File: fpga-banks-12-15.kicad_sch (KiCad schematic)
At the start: 1 part, among them U15 XC7K160T-FFG676

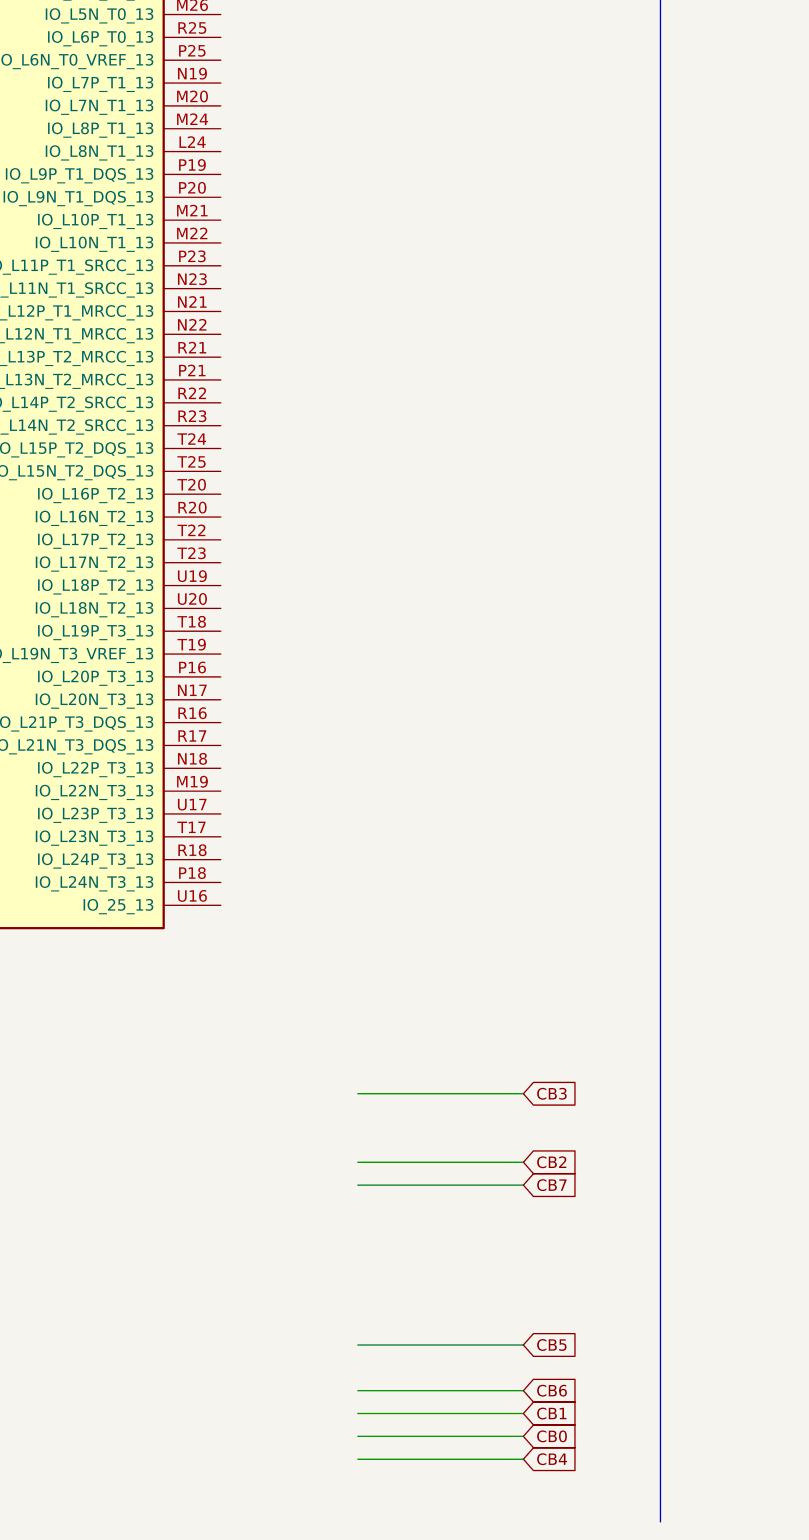
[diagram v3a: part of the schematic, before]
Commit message: Finish assigment and routing of ECC die
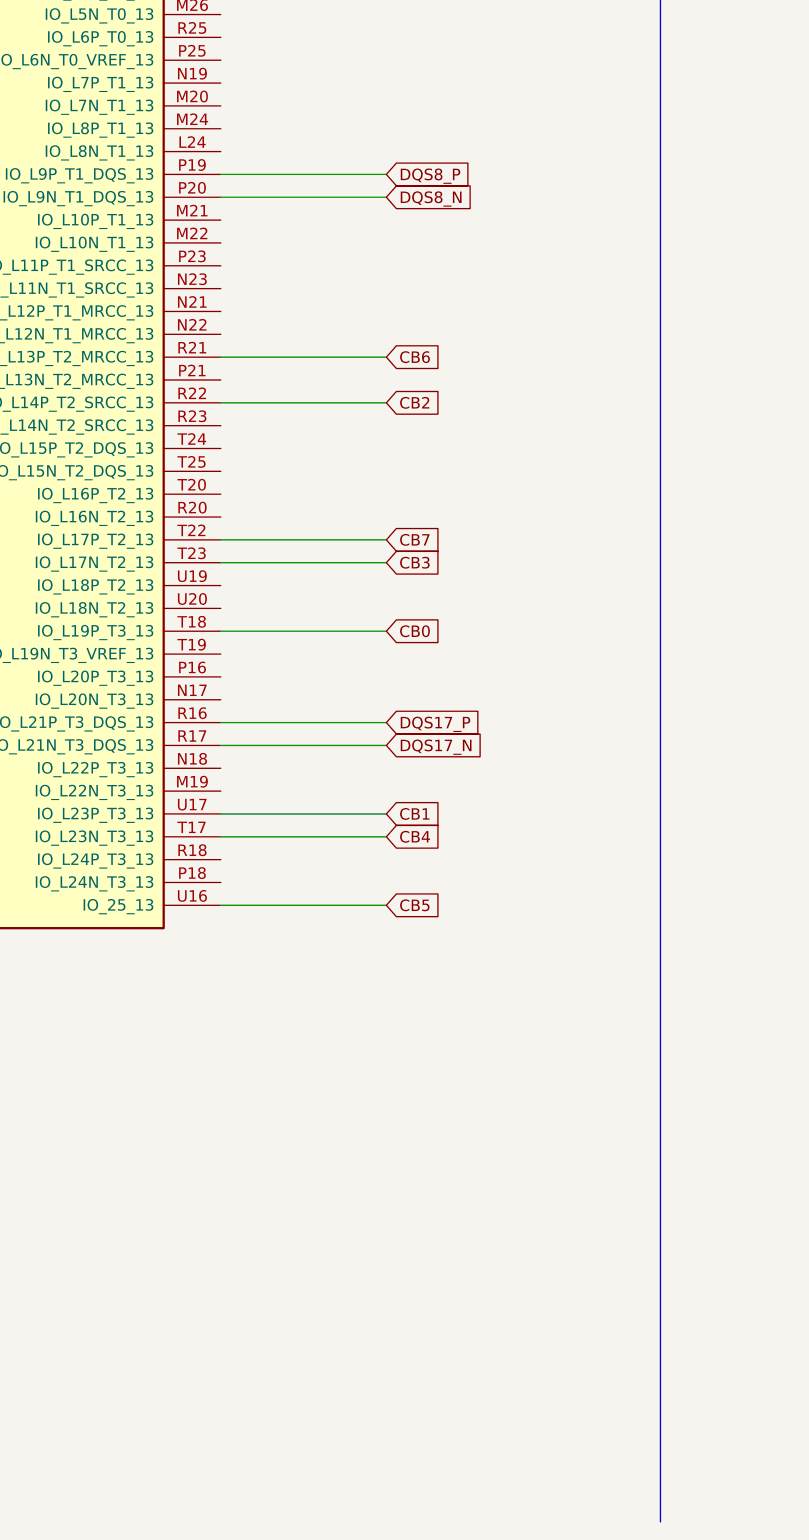
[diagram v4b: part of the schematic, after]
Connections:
- net CB0: now also U15.T18 (IO_L19P_T3_13)
- net CB1: now also U15.U17 (IO_L23P_T3_13)
- net CB2: now also U15.R22 (IO_L14P_T2_SRCC_13)
- net CB3: now also U15.T23 (IO_L17N_T2_13)
- net CB4: now also U15.T17 (IO_L23N_T3_13)
- net CB5: now also U15.U16 (IO_25_13)
- net CB6: now also U15.R21 (IO_L13P_T2_MRCC_13)
- net CB7: now also U15.T22 (IO_L17P_T2_13)
- net DQS8_P: now reaches U15.P19 (IO_L9P_T1_DQS_13)
- net DQS8_N: now reaches U15.P20 (IO_L9N_T1_DQS_13)
- net DQS17_P: now reaches U15.R16 (IO_L21P_T3_DQS_13)
- net DQS17_N: now reaches U15.R17 (IO_L21N_T3_DQS_13)
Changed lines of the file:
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@@
     (stroke (width 0) (type default) (color 0 0 0 0))
   )
-  (wire (pts (xy 176.53 278.13) (xy 194.945 278.13))
+  (wire (pts (xy 161.29 208.915) (xy 179.705 208.915))
     (stroke (width 0) (type default) (color 0 0 0 0))
   )
@@
     (stroke (width 0) (type default) (color 0 0 0 0))
   )
-  (wire (pts (xy 176.53 270.51) (xy 194.945 270.51))
+  (wire (pts (xy 161.29 155.575) (xy 179.705 155.575))
+    (stroke (width 0) (type default) (color 0 0 0 0))
+  )
+  (wire (pts (xy 161.29 135.255) (xy 179.705 135.255))
     (stroke (width 0) (type default) (color 0 0 0 0))
   )
@@
     (stroke (width 0) (type default) (color 0 0 0 0))
   )
+  (wire (pts (xy 161.29 198.755) (xy 179.705 198.755))
+    (stroke (width 0) (type default) (color 0 0 0 0))
+  )
   (wire (pts (xy 82.55 66.04) (xy 85.09 66.04))
     (stroke (width 0) (type default) (color 0 0 0 0))
@@
     (stroke (width 0) (type default) (color 0 0 0 0))
   )
-  (wire (pts (xy 176.53 275.59) (xy 194.945 275.59))
+  (wire (pts (xy 161.29 186.055) (xy 179.705 186.055))
     (stroke (width 0) (type default) (color 0 0 0 0))
   )
@@
     (stroke (width 0) (type default) (color 0 0 0 0))
   )
-  (wire (pts (xy 176.53 265.43) (xy 194.945 265.43))
+  (wire (pts (xy 161.29 216.535) (xy 179.705 216.535))
     (stroke (width 0) (type default) (color 0 0 0 0))
   )
@@
     (stroke (width 0) (type default) (color 0 0 0 0))
   )
+  (wire (pts (xy 161.29 137.795) (xy 179.705 137.795))
+    (stroke (width 0) (type default) (color 0 0 0 0))
+  )
   (wire (pts (xy 348.615 60.96) (xy 348.615 66.675))
     (stroke (width 0) (type default) (color 0 0 0 0))
@@
     (stroke (width 0) (type default) (color 0 0 0 0))
   )
-  (wire (pts (xy 176.53 247.65) (xy 194.945 247.65))
+  (wire (pts (xy 161.29 175.895) (xy 179.705 175.895))
     (stroke (width 0) (type default) (color 0 0 0 0))
   )
@@
     (stroke (width 0) (type default) (color 0 0 0 0))
   )
-  (wire (pts (xy 176.53 237.49) (xy 194.945 237.49))
+  (wire (pts (xy 161.29 178.435) (xy 179.705 178.435))
     (stroke (width 0) (type default) (color 0 0 0 0))
   )
@@
     (stroke (width 0) (type default) (color 0 0 0 0))
   )
+  (wire (pts (xy 161.29 196.215) (xy 179.705 196.215))
+    (stroke (width 0) (type default) (color 0 0 0 0))
+  )
   (wire (pts (xy 154.94 60.96) (xy 154.94 66.04))
     (stroke (width 0) (type default) (color 0 0 0 0))
@@
     (stroke (width 0) (type default) (color 0 0 0 0))
   )
-  (wire (pts (xy 176.53 245.11) (xy 194.945 245.11))
+  (wire (pts (xy 161.29 160.655) (xy 179.705 160.655))
     (stroke (width 0) (type default) (color 0 0 0 0))
   )
@@
     (stroke (width 0) (type default) (color 0 0 0 0))
   )
-  (wire (pts (xy 176.53 273.05) (xy 194.945 273.05))
+  (wire (pts (xy 161.29 206.375) (xy 179.705 206.375))
     (stroke (width 0) (type default) (color 0 0 0 0))
   )
@@
     )
   )
-  (global_label "CB6" (shape input) (at 194.945 270.51 0) (fields_autoplaced)
+  (global_label "CB6" (shape input) (at 179.705 155.575 0) (fields_autoplaced)
     (effects (font (size 1.27 1.27)) (justify left))
-    (property "Intersheet References" "${INTERSHEET_REFS}" (id 0) (at -177.165 76.835 0)
+    (property "Intersheet References" "${INTERSHEET_REFS}" (id 0) (at -192.405 -38.1 0)
       (effects (font (size 1.27 1.27)) hide)
     )
@@
     )
   )
-  (global_label "CB5" (shape input) (at 194.945 265.43 0) (fields_autoplaced)
+  (global_label "CB5" (shape input) (at 179.705 216.535 0) (fields_autoplaced)
     (effects (font (size 1.27 1.27)) (justify left))
-    (property "Intersheet References" "${INTERSHEET_REFS}" (id 0) (at -177.165 76.835 0)
+    (property "Intersheet References" "${INTERSHEET_REFS}" (id 0) (at -192.405 27.94 0)
       (effects (font (size 1.27 1.27)) hide)
     )
@@
     )
   )
-  (global_label "CB0" (shape input) (at 194.945 275.59 0) (fields_autoplaced)
+  (global_label "CB0" (shape input) (at 179.705 186.055 0) (fields_autoplaced)
     (effects (font (size 1.27 1.27)) (justify left))
-    (property "Intersheet References" "${INTERSHEET_REFS}" (id 0) (at -177.165 76.835 0)
+    (property "Intersheet References" "${INTERSHEET_REFS}" (id 0) (at -192.405 -12.7 0)
       (effects (font (size 1.27 1.27)) hide)
     )
@@
     )
   )
-  (global_label "CB7" (shape input) (at 194.945 247.65 0) (fields_autoplaced)
+  (global_label "CB7" (shape input) (at 179.705 175.895 0) (fields_autoplaced)
     (effects (font (size 1.27 1.27)) (justify left))
-    (property "Intersheet References" "${INTERSHEET_REFS}" (id 0) (at -177.165 76.835 0)
+    (property "Intersheet References" "${INTERSHEET_REFS}" (id 0) (at -192.405 5.08 0)
       (effects (font (size 1.27 1.27)) hide)
     )
@@
     (property "Intersheet References" "${INTERSHEET_REFS}" (id 0) (at 0 0 0)
       (effects (font (size 1.27 1.27)) hide)
+    )
+  )
+  (global_label "DQS17_N" (shape input) (at 179.705 198.755 0) (fields_autoplaced)
+    (effects (font (size 1.27 1.27)) (justify left))
+    (property "Intersheet References" "${INTERSHEET_REFS}" (id 0) (at 190.5563 198.6756 0)
+      (effects (font (size 1.27 1.27)) (justify left) hide)
     )
   )
@@
     )
   )
+  (global_label "DQS8_N" (shape input) (at 179.705 137.795 0) (fields_autoplaced)
+    (effects (font (size 1.27 1.27)) (justify left))
+    (property "Intersheet References" "${INTERSHEET_REFS}" (id 0) (at 189.3468 137.7156 0)
+      (effects (font (size 1.27 1.27)) (justify left) hide)
+    )
+  )
   (global_label "HR_DQ7" (shape input) (at 59.69 173.355 180) (fields_autoplaced)
     (effects (font (size 1.27 1.27)) (justify right))
@@
     )
   )
-  (global_label "CB4" (shape input) (at 194.945 278.13 0) (fields_autoplaced)
+  (global_label "CB4" (shape input) (at 179.705 208.915 0) (fields_autoplaced)
     (effects (font (size 1.27 1.27)) (justify left))
-    (property "Intersheet References" "${INTERSHEET_REFS}" (id 0) (at -177.165 76.835 0)
-      (effects (font (size 1.27 1.27)) hide)
-    )
-  )
-  (global_label "CB2" (shape input) (at 194.945 245.11 0) (fields_autoplaced)
+    (property "Intersheet References" "${INTERSHEET_REFS}" (id 0) (at -192.405 7.62 0)
+      (effects (font (size 1.27 1.27)) hide)
+    )
+  )
+  (global_label "CB2" (shape input) (at 179.705 160.655 0) (fields_autoplaced)
     (effects (font (size 1.27 1.27)) (justify left))
-    (property "Intersheet References" "${INTERSHEET_REFS}" (id 0) (at -177.165 76.835 0)
+    (property "Intersheet References" "${INTERSHEET_REFS}" (id 0) (at -192.405 -7.62 0)
       (effects (font (size 1.27 1.27)) hide)
     )
@@
     )
   )
+  (global_label "DQS17_P" (shape input) (at 179.705 196.215 0) (fields_autoplaced)
+    (effects (font (size 1.27 1.27)) (justify left))
+    (property "Intersheet References" "${INTERSHEET_REFS}" (id 0) (at 190.4959 196.1356 0)
+      (effects (font (size 1.27 1.27)) (justify left) hide)
+    )
+  )
   (global_label "USR_LED2" (shape input) (at 253.365 130.81 180) (fields_autoplaced)
     (effects (font (size 1.27 1.27)) (justify right))
@@
     )
   )
-  (global_label "CB1" (shape input) (at 194.945 273.05 0) (fields_autoplaced)
+  (global_label "CB1" (shape input) (at 179.705 206.375 0) (fields_autoplaced)
     (effects (font (size 1.27 1.27)) (justify left))
-    (property "Intersheet References" "${INTERSHEET_REFS}" (id 0) (at -177.165 76.835 0)
+    (property "Intersheet References" "${INTERSHEET_REFS}" (id 0) (at -192.405 10.16 0)
       (effects (font (size 1.27 1.27)) hide)
     )
@@
     )
   )
-  (global_label "CB3" (shape input) (at 194.945 237.49 0) (fields_autoplaced)
+  (global_label "CB3" (shape input) (at 179.705 178.435 0) (fields_autoplaced)
     (effects (font (size 1.27 1.27)) (justify left))
-    (property "Intersheet References" "${INTERSHEET_REFS}" (id 0) (at -177.165 76.835 0)
+    (property "Intersheet References" "${INTERSHEET_REFS}" (id 0) (at -192.405 17.78 0)
       (effects (font (size 1.27 1.27)) hide)
     )
@@
     )
   )
+  (global_label "DQS8_P" (shape input) (at 179.705 135.255 0) (fields_autoplaced)
+    (effects (font (size 1.27 1.27)) (justify left))
+    (property "Intersheet References" "${INTERSHEET_REFS}" (id 0) (at 189.2863 135.1756 0)
+      (effects (font (size 1.27 1.27)) (justify left) hide)
+    )
+  )

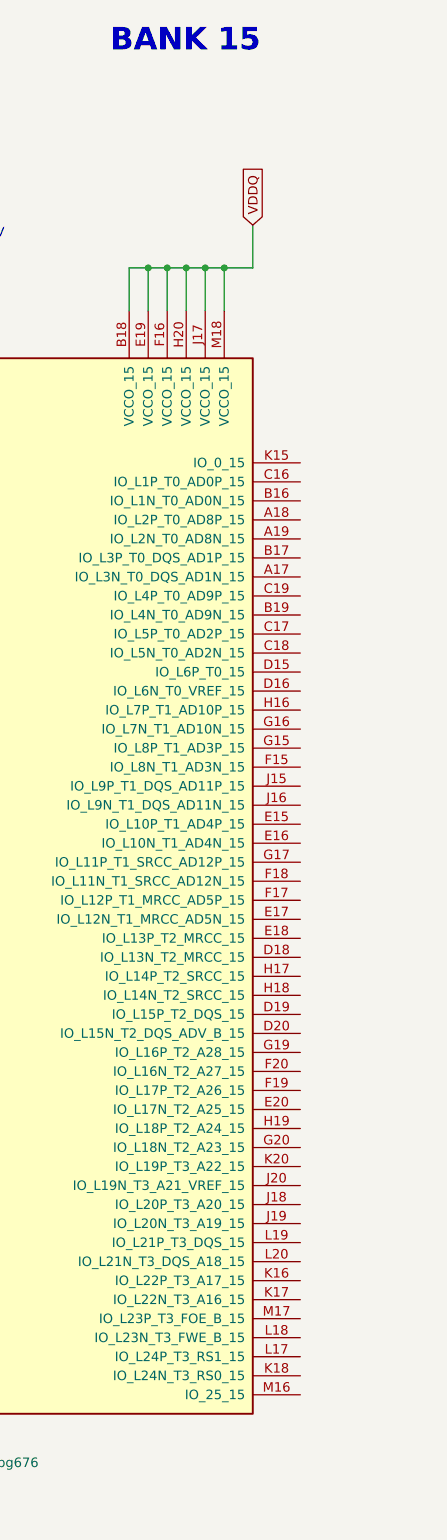
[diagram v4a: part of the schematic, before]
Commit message: Implement LED and PB mechanical concept. Assign bank 15 to FMC, remove buttons and add new ones
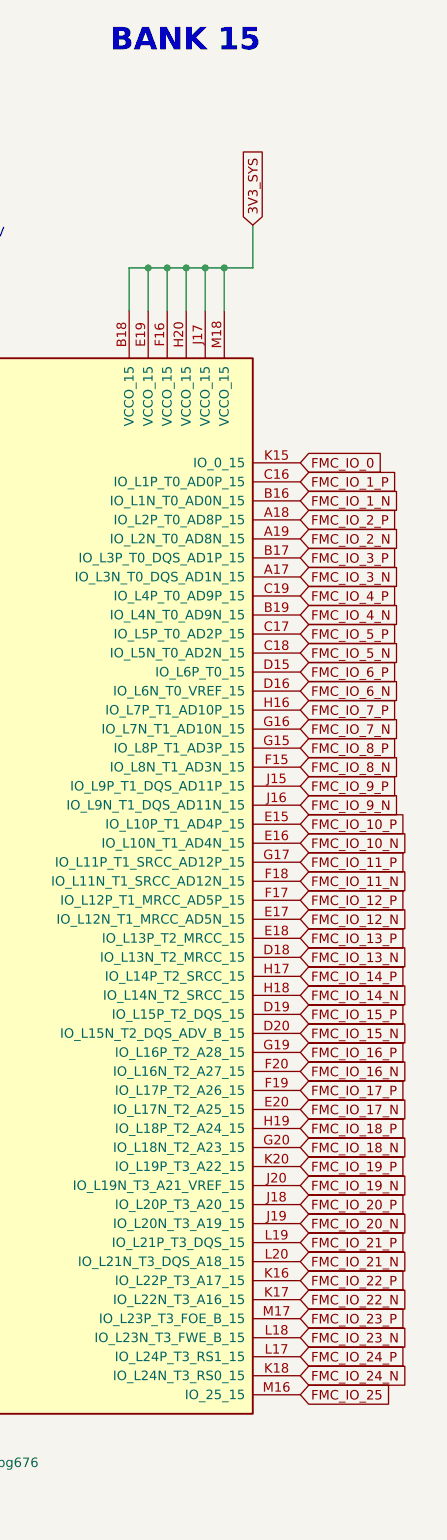
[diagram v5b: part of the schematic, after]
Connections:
- net 3V3_SYS: now also U15.B18 (VCCO_15), U15.E19 (VCCO_15), U15.F16 (VCCO_15), U15.H20 (VCCO_15), U15.J17 (VCCO_15), U15.M18 (VCCO_15)
- net VDDQ: no longer U15.B18 (VCCO_15), U15.E19 (VCCO_15), U15.F16 (VCCO_15), U15.H20 (VCCO_15), U15.J17 (VCCO_15), U15.M18 (VCCO_15)
- net FMC_IO_3_N: now reaches U15.A17 (IO_L3N_T0_DQS_AD1N_15)
- net FMC_IO_2_P: now reaches U15.A18 (IO_L2P_T0_AD8P_15)
- net FMC_IO_2_N: now reaches U15.A19 (IO_L2N_T0_AD8N_15)
- net FMC_IO_1_N: now reaches U15.B16 (IO_L1N_T0_AD0N_15)
- net FMC_IO_3_P: now reaches U15.B17 (IO_L3P_T0_DQS_AD1P_15)
- net FMC_IO_4_N: now reaches U15.B19 (IO_L4N_T0_AD9N_15)
- net FMC_IO_1_P: now reaches U15.C16 (IO_L1P_T0_AD0P_15)
- net FMC_IO_5_P: now reaches U15.C17 (IO_L5P_T0_AD2P_15)
- net FMC_IO_5_N: now reaches U15.C18 (IO_L5N_T0_AD2N_15)
- net FMC_IO_4_P: now reaches U15.C19 (IO_L4P_T0_AD9P_15)
- net FMC_IO_6_P: now reaches U15.D15 (IO_L6P_T0_15)
- net FMC_IO_6_N: now reaches U15.D16 (IO_L6N_T0_VREF_15)
- net FMC_IO_13_N: now reaches U15.D18 (IO_L13N_T2_MRCC_15)
- net FMC_IO_15_P: now reaches U15.D19 (IO_L15P_T2_DQS_15)
- net FMC_IO_15_N: now reaches U15.D20 (IO_L15N_T2_DQS_ADV_B_15)
- net FMC_IO_10_P: now reaches U15.E15 (IO_L10P_T1_AD4P_15)
- net FMC_IO_10_N: now reaches U15.E16 (IO_L10N_T1_AD4N_15)
- net FMC_IO_12_N: now reaches U15.E17 (IO_L12N_T1_MRCC_AD5N_15)
- net FMC_IO_13_P: now reaches U15.E18 (IO_L13P_T2_MRCC_15)
- net FMC_IO_17_N: now reaches U15.E20 (IO_L17N_T2_A25_15)
- net FMC_IO_8_N: now reaches U15.F15 (IO_L8N_T1_AD3N_15)
- net FMC_IO_12_P: now reaches U15.F17 (IO_L12P_T1_MRCC_AD5P_15)
- net FMC_IO_11_N: now reaches U15.F18 (IO_L11N_T1_SRCC_AD12N_15)
- net FMC_IO_17_P: now reaches U15.F19 (IO_L17P_T2_A26_15)
- net FMC_IO_16_N: now reaches U15.F20 (IO_L16N_T2_A27_15)
- net FMC_IO_8_P: now reaches U15.G15 (IO_L8P_T1_AD3P_15)
- net FMC_IO_7_N: now reaches U15.G16 (IO_L7N_T1_AD10N_15)
- net FMC_IO_11_P: now reaches U15.G17 (IO_L11P_T1_SRCC_AD12P_15)
- net FMC_IO_16_P: now reaches U15.G19 (IO_L16P_T2_A28_15)
- net FMC_IO_18_N: now reaches U15.G20 (IO_L18N_T2_A23_15)
- net FMC_IO_7_P: now reaches U15.H16 (IO_L7P_T1_AD10P_15)
- net FMC_IO_14_P: now reaches U15.H17 (IO_L14P_T2_SRCC_15)
- net FMC_IO_14_N: now reaches U15.H18 (IO_L14N_T2_SRCC_15)
- net FMC_IO_18_P: now reaches U15.H19 (IO_L18P_T2_A24_15)
- net FMC_IO_9_P: now reaches U15.J15 (IO_L9P_T1_DQS_AD11P_15)
- net FMC_IO_9_N: now reaches U15.J16 (IO_L9N_T1_DQS_AD11N_15)
- net FMC_IO_20_P: now reaches U15.J18 (IO_L20P_T3_A20_15)
- net FMC_IO_20_N: now reaches U15.J19 (IO_L20N_T3_A19_15)
- net FMC_IO_19_N: now reaches U15.J20 (IO_L19N_T3_A21_VREF_15)
- net FMC_IO_0: now reaches U15.K15 (IO_0_15)
- net FMC_IO_22_P: now reaches U15.K16 (IO_L22P_T3_A17_15)
- net FMC_IO_22_N: now reaches U15.K17 (IO_L22N_T3_A16_15)
- net FMC_IO_24_N: now reaches U15.K18 (IO_L24N_T3_RS0_15)
- net FMC_IO_19_P: now reaches U15.K20 (IO_L19P_T3_A22_15)
- net FMC_IO_24_P: now reaches U15.L17 (IO_L24P_T3_RS1_15)
- net FMC_IO_23_N: now reaches U15.L18 (IO_L23N_T3_FWE_B_15)
- net FMC_IO_21_P: now reaches U15.L19 (IO_L21P_T3_DQS_15)
- net FMC_IO_21_N: now reaches U15.L20 (IO_L21N_T3_DQS_A18_15)
- net FMC_IO_25: now reaches U15.M16 (IO_25_15)
- net FMC_IO_23_P: now reaches U15.M17 (IO_L23P_T3_FOE_B_15)
